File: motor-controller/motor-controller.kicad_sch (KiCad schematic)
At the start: 36 parts, among them J1 Motor0, J2 Motor1, J3 BATT, J4 MCU, U2 LT1161

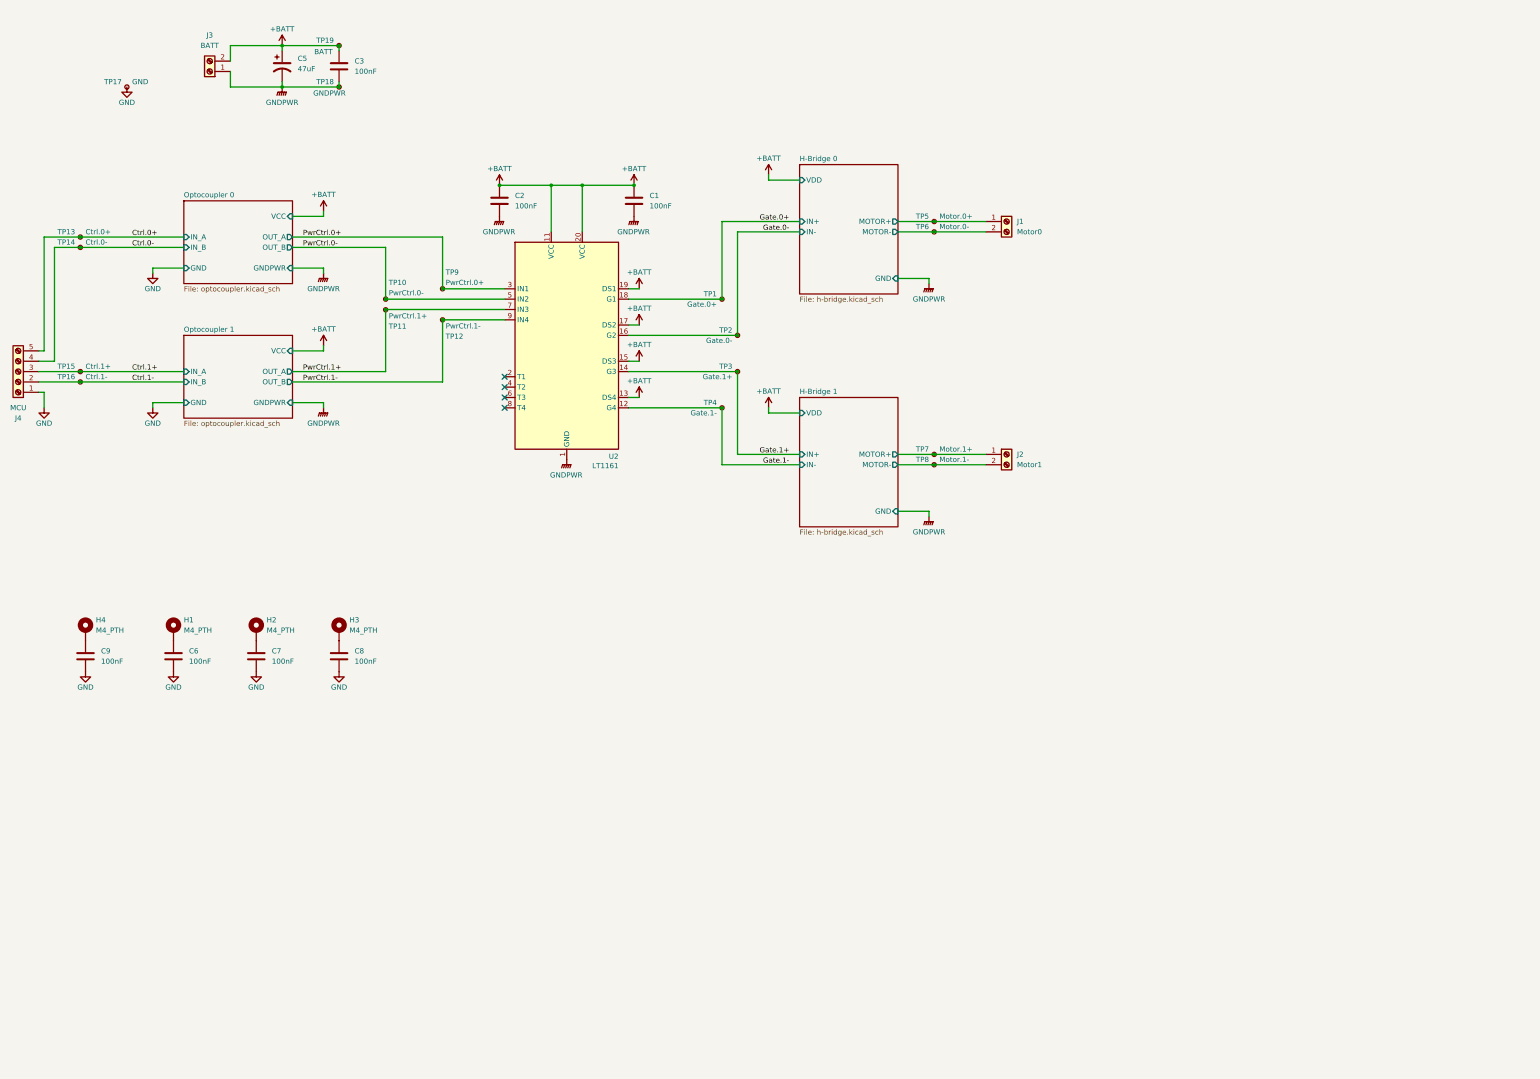
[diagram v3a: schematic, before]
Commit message: Change h-bridge design to newer version
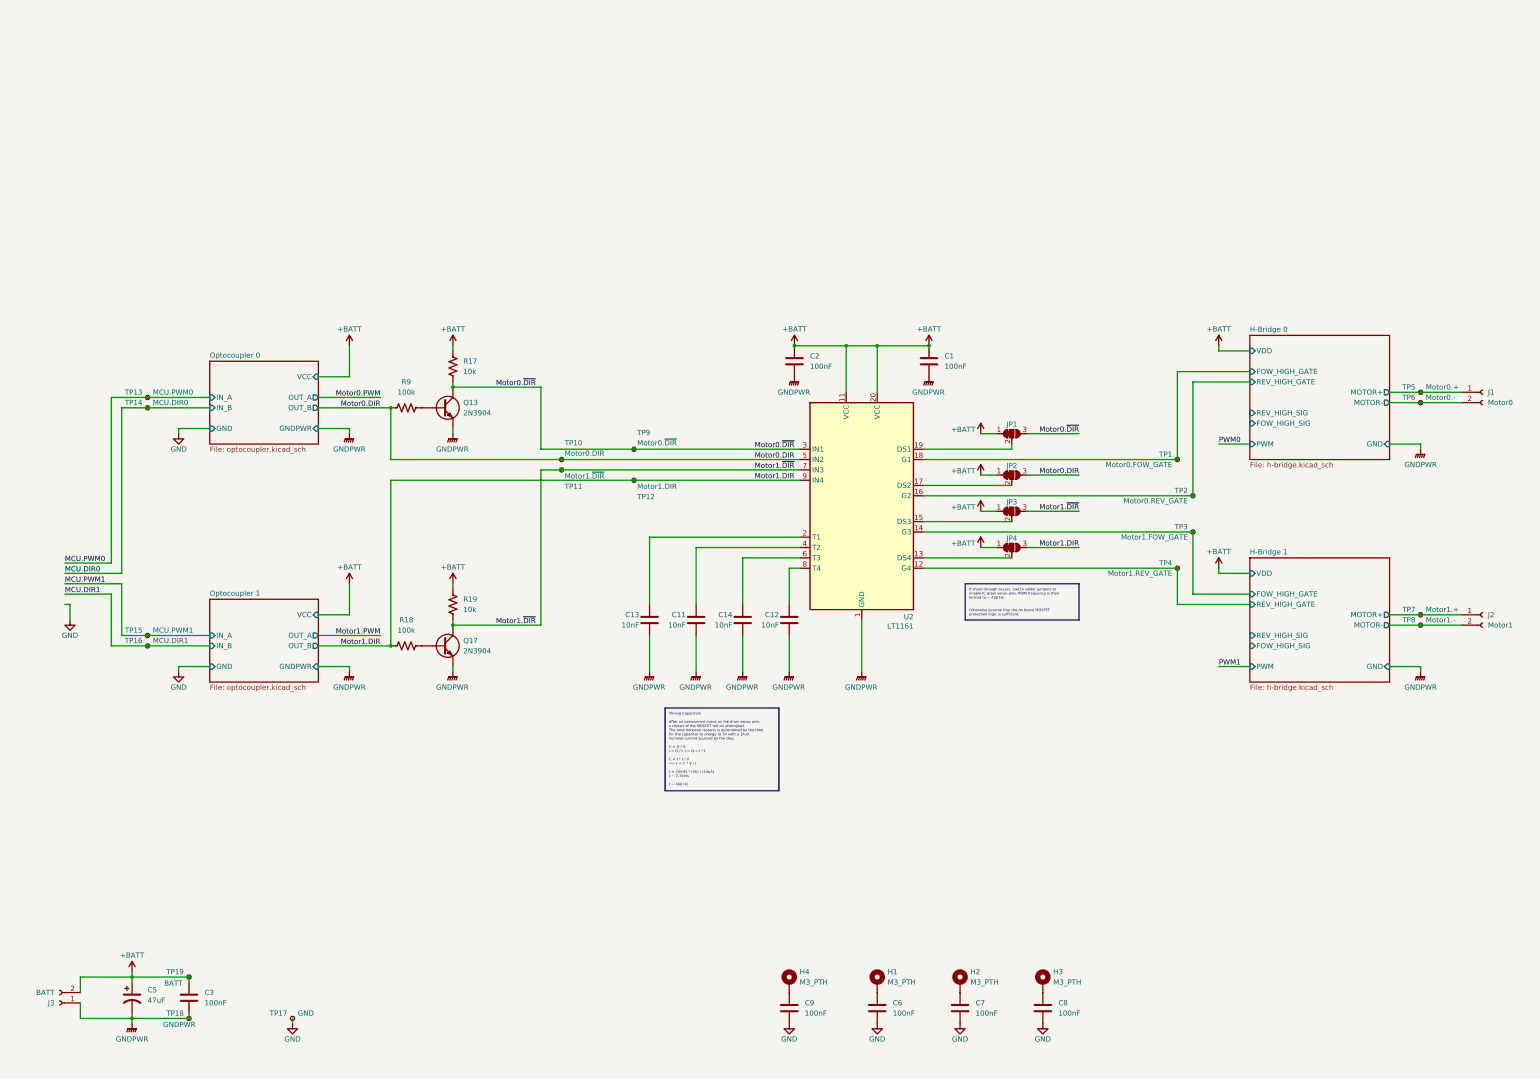
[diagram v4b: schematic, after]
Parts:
- removed J1: Motor0, TerminalBlock:TerminalBlock_MaiXu_MX126-5.0-02P_1x02_P5.00mm, symbol Connector:Screw_Terminal_01x02
- removed J2: Motor1, TerminalBlock:TerminalBlock_MaiXu_MX126-5.0-02P_1x02_P5.00mm, symbol Connector:Screw_Terminal_01x02
- removed J3: BATT, TerminalBlock:TerminalBlock_MaiXu_MX126-5.0-02P_1x02_P5.00mm, symbol Connector:Screw_Terminal_01x02
- removed J4: MCU, TerminalBlock:TerminalBlock_Xinya_XY308-2.54-5P_1x05_P2.54mm_Horizontal, symbol Connector:Screw_Terminal_01x05
- added C11, C12, C13, C14: 10nF, Capacitor_THT:C_Disc_D3.0mm_W2.0mm_P2.50mm, symbol GS_Capacitor_THT:C_THT_100nF
- added J1: Motor0, Connector_JST:JST_XH_B2B-XH-A_1x02_P2.50mm_Vertical, symbol Connector:Conn_01x02_Socket
- added J2: Motor1, Connector_JST:JST_XH_B2B-XH-A_1x02_P2.50mm_Vertical, symbol Connector:Conn_01x02_Socket
- added J3: BATT, Connector_JST:JST_XH_B2B-XH-A_1x02_P2.50mm_Vertical, symbol Connector:Conn_01x02_Socket
- added JP1, JP2, JP3, JP4: VALUE, Jumper:SolderJumper-3_P1.3mm_Bridged12_RoundedPad1.0x1.5mm, symbol GS_Virtual:SolderJumper_3_Bridged12
- added Q13, Q17: 2N3904, Package_TO_SOT_THT:TO-92_Inline, symbol GS_Transistors:BJT_NPN_40V_200mA
- added R17, R19: 10k, Resistor_THT:R_Axial_DIN0309_L9.0mm_D3.2mm_P12.70mm_Horizontal, symbol GS_Resistor_THT:R_250mW
- added R18, R9: 100k, Resistor_THT:R_Axial_DIN0309_L9.0mm_D3.2mm_P12.70mm_Horizontal, symbol GS_Resistor_THT:R_250mW
- C5: footprint Capacitor_THT:C_Radial_D5.0mm_H11.0mm_P2.00mm -> Capacitor_THT:CP_Radial_D5.0mm_P2.00mm
- H1, H2, H3, H4: value M4_PTH -> M3_PTH; footprint MountingHole:MountingHole_4.3mm_M4_Pad -> MountingHole:MountingHole_3.2mm_M3_Pad
- TP1: value Gate.0+ -> Motor0.FOW_GATE
- TP10: value PwrCtrl.0- -> Motor0.DIR
- TP11: value PwrCtrl.1+ -> Motor1.~{DIR}
- TP12: value PwrCtrl.1- -> Motor1.DIR
- TP13: value Ctrl.0+ -> MCU.PWM0
- TP14: value Ctrl.0- -> MCU.DIR0
- TP15: value Ctrl.1+ -> MCU.PWM1
- TP16: value Ctrl.1- -> MCU.DIR1
- TP2: value Gate.0- -> Motor0.REV_GATE
- TP3: value Gate.1+ -> Motor1.FOW_GATE
- TP4: value Gate.1- -> Motor1.REV_GATE
- TP5: value Motor.0+ -> Motor0.+
- TP6: value Motor.0- -> Motor0.-
- TP7: value Motor.1+ -> Motor1.+
- TP8: value Motor.1- -> Motor1.-
- TP9: value PwrCtrl.0+ -> Motor0.~{DIR}
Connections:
- net +BATT: now also J3.2 (Pin_2), JP1.1 (A), JP2.1 (A), JP3.1 (A), JP4.1 (A), R17.1, R19.1; no longer U2.13 (DS4), U2.15 (DS3), U2.17 (DS2), U2.19 (DS1)
- net GND: now also C11.2, C12.2, C13.2, C14.2, J3.1 (Pin_1), Q13.E, Q17.E
- net H-Bridge 0/MOTOR+: now also J1.1 (Pin_1)
- net H-Bridge 0/MOTOR-: now also J1.2 (Pin_2)
- net H-Bridge 1/MOTOR+: now also J2.1 (Pin_1)
- net H-Bridge 1/MOTOR-: now also J2.2 (Pin_2)
- net at U2.2 (T1): now also C13.1
- net at U2.4 (T2): now also C11.1
- net at U2.6 (T3): now also C14.1
- net at U2.8 (T4): now also C12.1
- net Ctrl.0+ renamed MCU.PWM0
- net Ctrl.0- renamed MCU.DIR0
- net Ctrl.1+ renamed MCU.PWM1
- net Ctrl.1- renamed MCU.DIR1
- net Gate.0+ renamed H-Bridge 0/FOW_HIGH_GATE
- net Gate.0- renamed H-Bridge 0/REV_HIGH_GATE
- net Gate.1+ renamed H-Bridge 1/FOW_HIGH_GATE
- net Gate.1- renamed H-Bridge 1/REV_HIGH_GATE
- net PwrCtrl.0+ renamed Motor0.~{DIR}
- net Motor0.~{DIR}: now also JP1.3 (B), Q13.C, R17.2
- net PwrCtrl.0- renamed Motor0.DIR
- net Motor0.DIR: now also JP2.3 (B), R9.1
- net PwrCtrl.1+ renamed Motor1.~{DIR}
- net Motor1.~{DIR}: now also JP3.3 (B), Q17.C, R19.2
- net PwrCtrl.1- renamed Motor1.DIR
- net Motor1.DIR: now also JP4.3 (B), R18.1
- new net: JP3.2 (C), U2.15 (DS3)
- new net: Q17.B, R18.2
- new net: JP4.2 (C), U2.13 (DS4)
- new net: JP2.2 (C), U2.17 (DS2)
- new net: JP1.2 (C), U2.19 (DS1)
- new net: Q13.B, R9.2
- no-connect marks 4 -> 0
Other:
- sheet H-Bridge 0 ports: added FOW_HIGH_GATE, FOW_HIGH_SIG, PWM, REV_HIGH_GATE, REV_HIGH_SIG; removed IN+, IN-
- sheet H-Bridge 1 ports: added FOW_HIGH_GATE, FOW_HIGH_SIG, PWM, REV_HIGH_GATE, REV_HIGH_SIG; removed IN+, IN-
- moved on the sheet: C1, C2, C3, C5, C6, C7, C8, C9, H1, H2, H3, H4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

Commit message: Fix some ERC issues
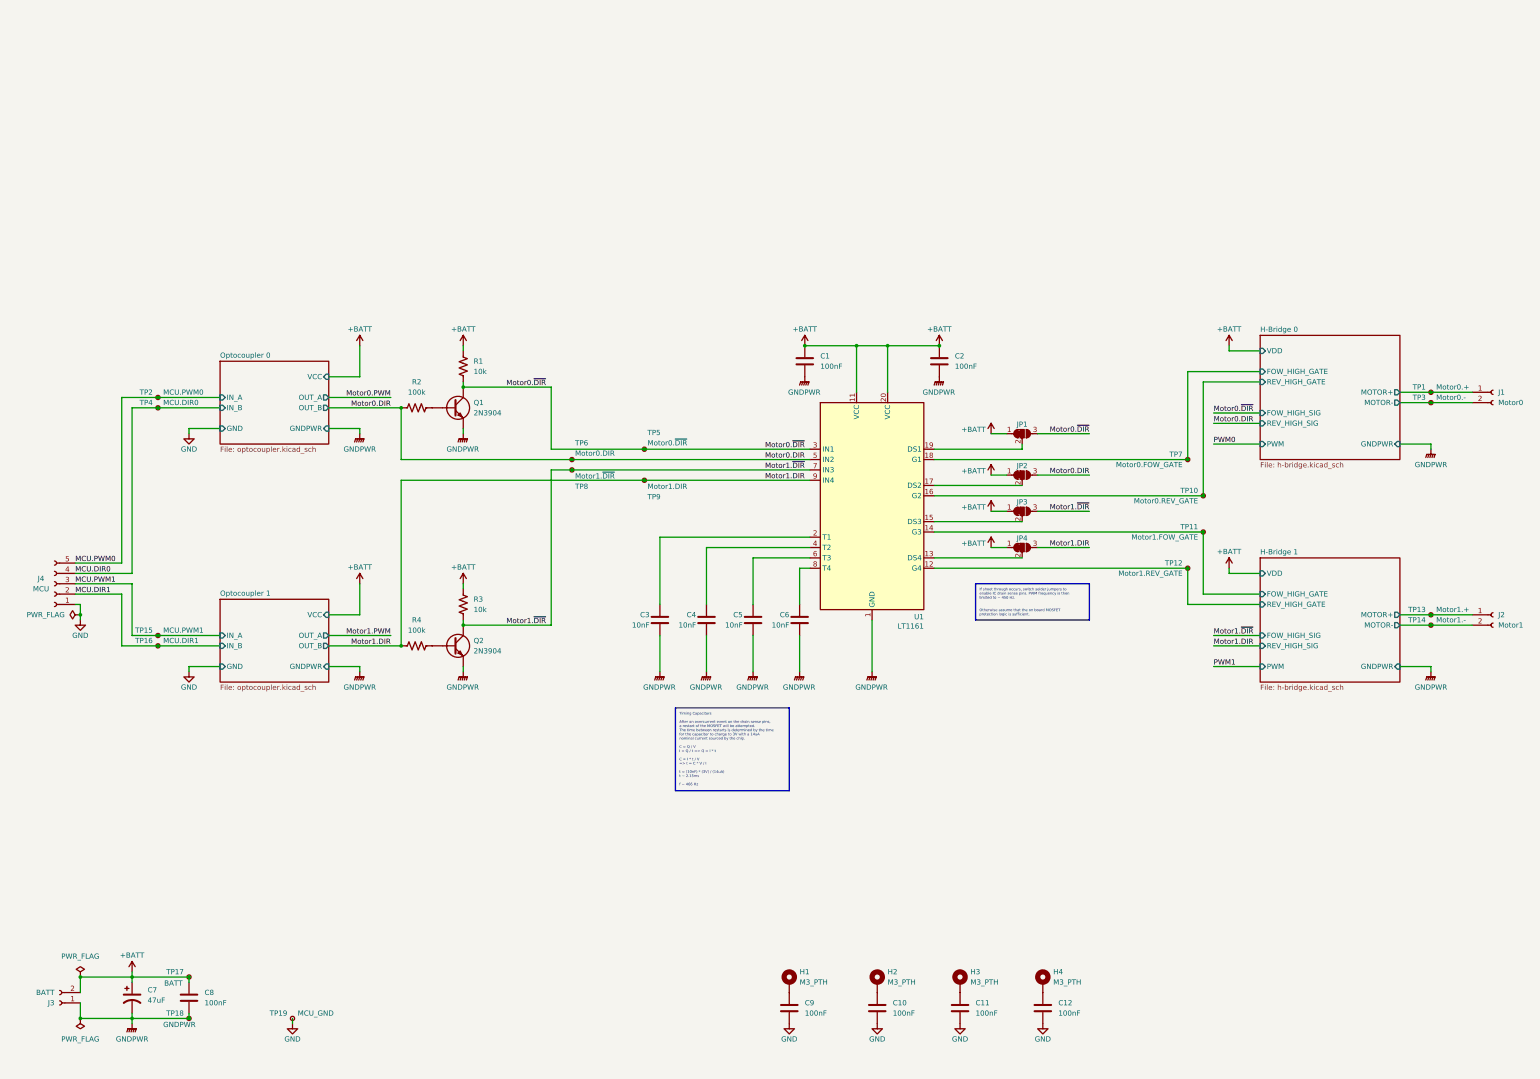
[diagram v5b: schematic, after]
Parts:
- added J4: MCU, Connector_JST:JST_XH_B5B-XH-A_1x05_P2.50mm_Vertical, symbol Connector:Conn_01x05_Socket
- JP1: value VALUE -> Motor0_FOW
- JP2: value VALUE -> MOTOR0_REV
- JP3: value VALUE -> MOTOR1_FOW
- JP4: value VALUE -> MOTOR1_REV
- TP19: renamed from TP17; value GND -> MCU_GND
- renumbered C2 to C1, C6 to C10, C7 to C11, C8 to C12, C1 to C2, C13 to C3, C11 to C4, C14 to C5, C12 to C6, C5 to C7, C3 to C8, H4 to H1, H1 to H2, H2 to H3, H3 to H4, Q13 to Q1, Q17 to Q2, R17 to R1, R9 to R2, R19 to R3, R18 to R4, TP5 to TP1, TP2 to TP10, TP3 to TP11, TP4 to TP12, TP7 to TP13, TP8 to TP14, TP19 to TP17, TP13 to TP2, TP6 to TP3, TP14 to TP4, TP9 to TP5, TP10 to TP6, TP1 to TP7, TP11 to TP8, TP12 to TP9, U2 to U1
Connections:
- net GND: now also J4.1 (Pin_1); no longer C1.2, C2.2, C3.2, C4.2, C5.2, C6.2, C7.2, C8.2, J3.1 (Pin_1), Q1.E, Q2.E, TP18.1, U1.1 (GND), U1.10 (GND)
- net MCU.DIR0: now also J4.4 (Pin_4)
- net MCU.DIR1: now also J4.2 (Pin_2)
- net MCU.PWM0: now also J4.5 (Pin_5)
- net MCU.PWM1: now also J4.3 (Pin_3)
- net Motor0.~{DIR}: now also Q1.3 (C); no longer Q1.C
- net Motor1.~{DIR}: now also Q2.3 (C); no longer Q2.C
- net at R4.2: now also Q2.2 (B); no longer Q2.B
- net at R2.2: now also Q1.2 (B); no longer Q1.B
- new net GNDPWR: C1.2, C2.2, C3.2, C4.2, C5.2, C6.2, C7.2, C8.2, J3.1 (Pin_1), Q1.1 (E), Q2.1 (E), TP18.1, U1.1 (GND), U1.10 (GND)
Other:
- sheet H-Bridge 0 ports: added GNDPWR; removed GND
- sheet H-Bridge 1 ports: added GNDPWR; removed GND
- moved on the sheet: C1, C2, C3, C4, C5, C6, J1, J2, JP1, JP2, JP3, JP4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
